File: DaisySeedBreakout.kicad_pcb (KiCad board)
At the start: 2 copper layers, 56.1 x 65 mm, 200 parts, among them J1 Conn_01x03, J10 Conn_01x02, J11 Conn_01x02, J12 Conn_01x02, J13 Conn_01x02, J14 Conn_01x02, J2 Conn_01x02, J20 Conn_01x02, J21 Conn_01x02, J22 Conn_01x02, J24 Conn_01x02, J25 Conn_01x02, J26 Conn_02x04, J27 Conn_01x03, J3 Conn_01x03, J30 Conn_01x02, J31 Conn_02x04, J32 Conn_01x02, J33 Conn_01x02, J34 Conn_01x02, J35 Conn_01x02, J4 5027740891, J47 Conn_01x03, J48 Conn_01x03, J49 Conn_01x03, J50 Conn_01x03, J51 Conn_01x03, J52 Conn_01x03, J53 Conn_01x03, J54 Conn_01x03, J55 Conn_01x03, J56 Conn_01x03, J57 Conn_01x03, J58 Conn_01x03, J59 Conn_01x03, J6 Conn_01x02, J60 Conn_01x03, J61 Conn_01x03, J62 Conn_01x03, J63 Conn_01x03, J64 Conn_01x03, J65 Conn_01x03, J67 Conn_01x02, J68 Conn_01x02, J69 Conn_01x02, J70 Conn_01x02, J8 Conn_01x02, J9 Conn_01x02, U1 H11L1M, U10 TPD2EUSB30ADRTR, U11 TPS560200DBVR, U2 PAM8320RDR, U4 ATMEGA1608-MFR, U5 MAX9814, U6 DSC6001CE2A-010.0000, U7 TLV9062IDR

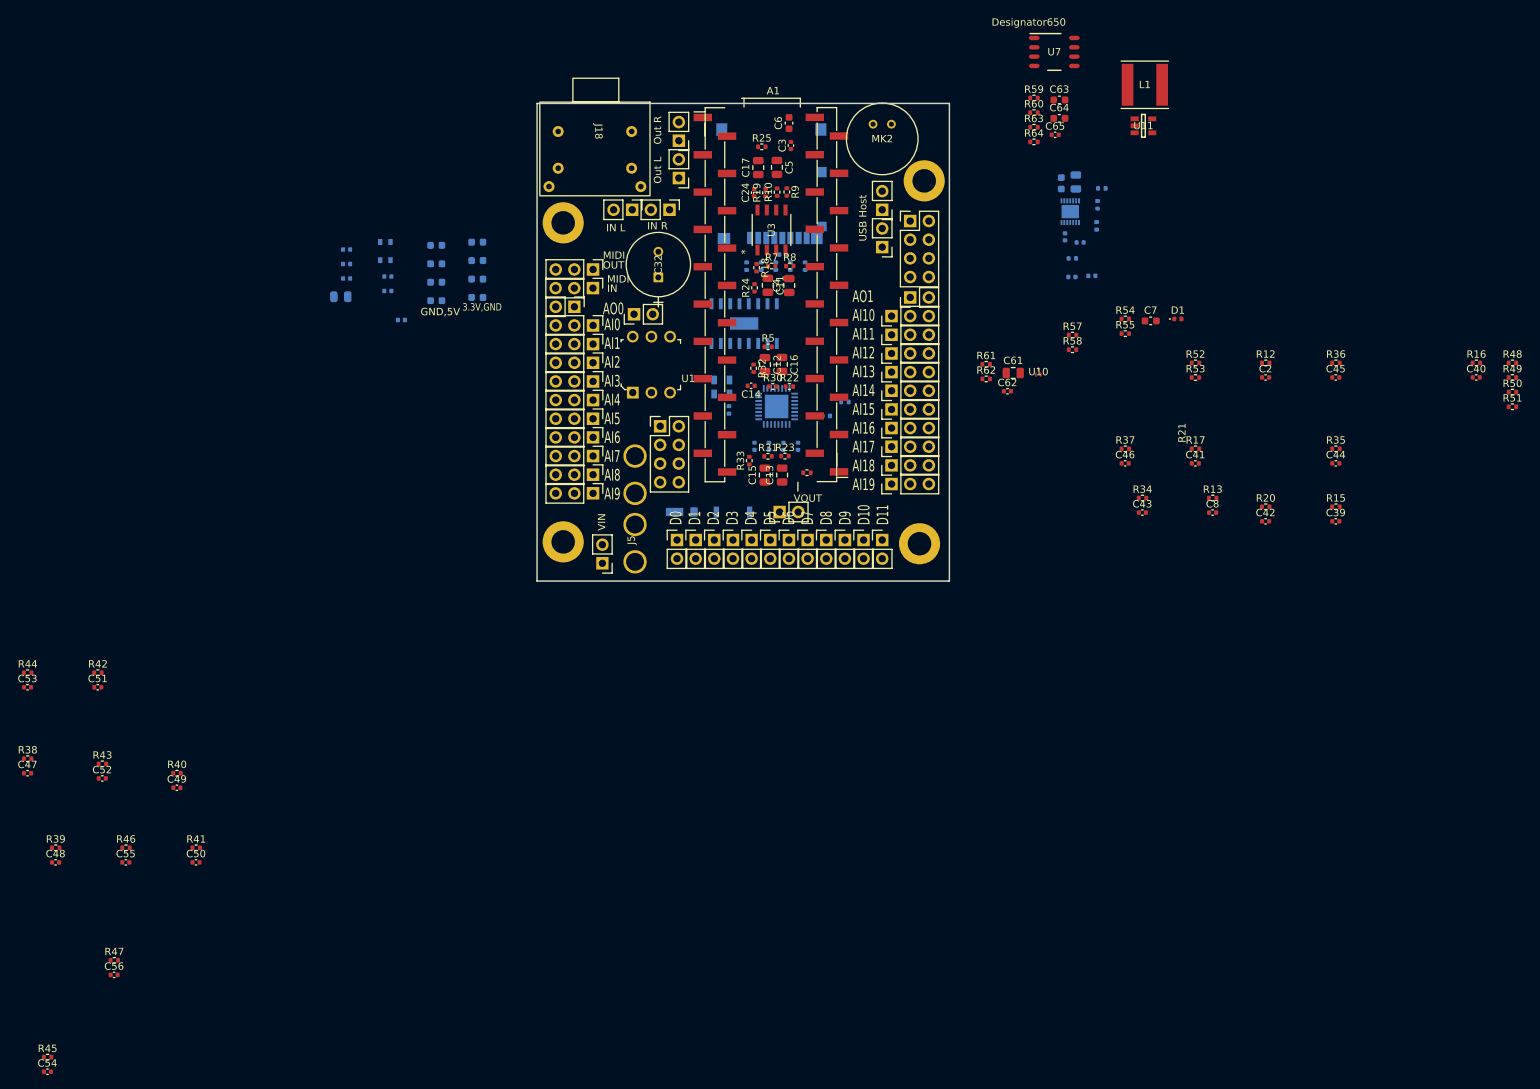
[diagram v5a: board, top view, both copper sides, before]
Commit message: Update Audio out to switch between 1V ptp or 10V ptp based on jumper
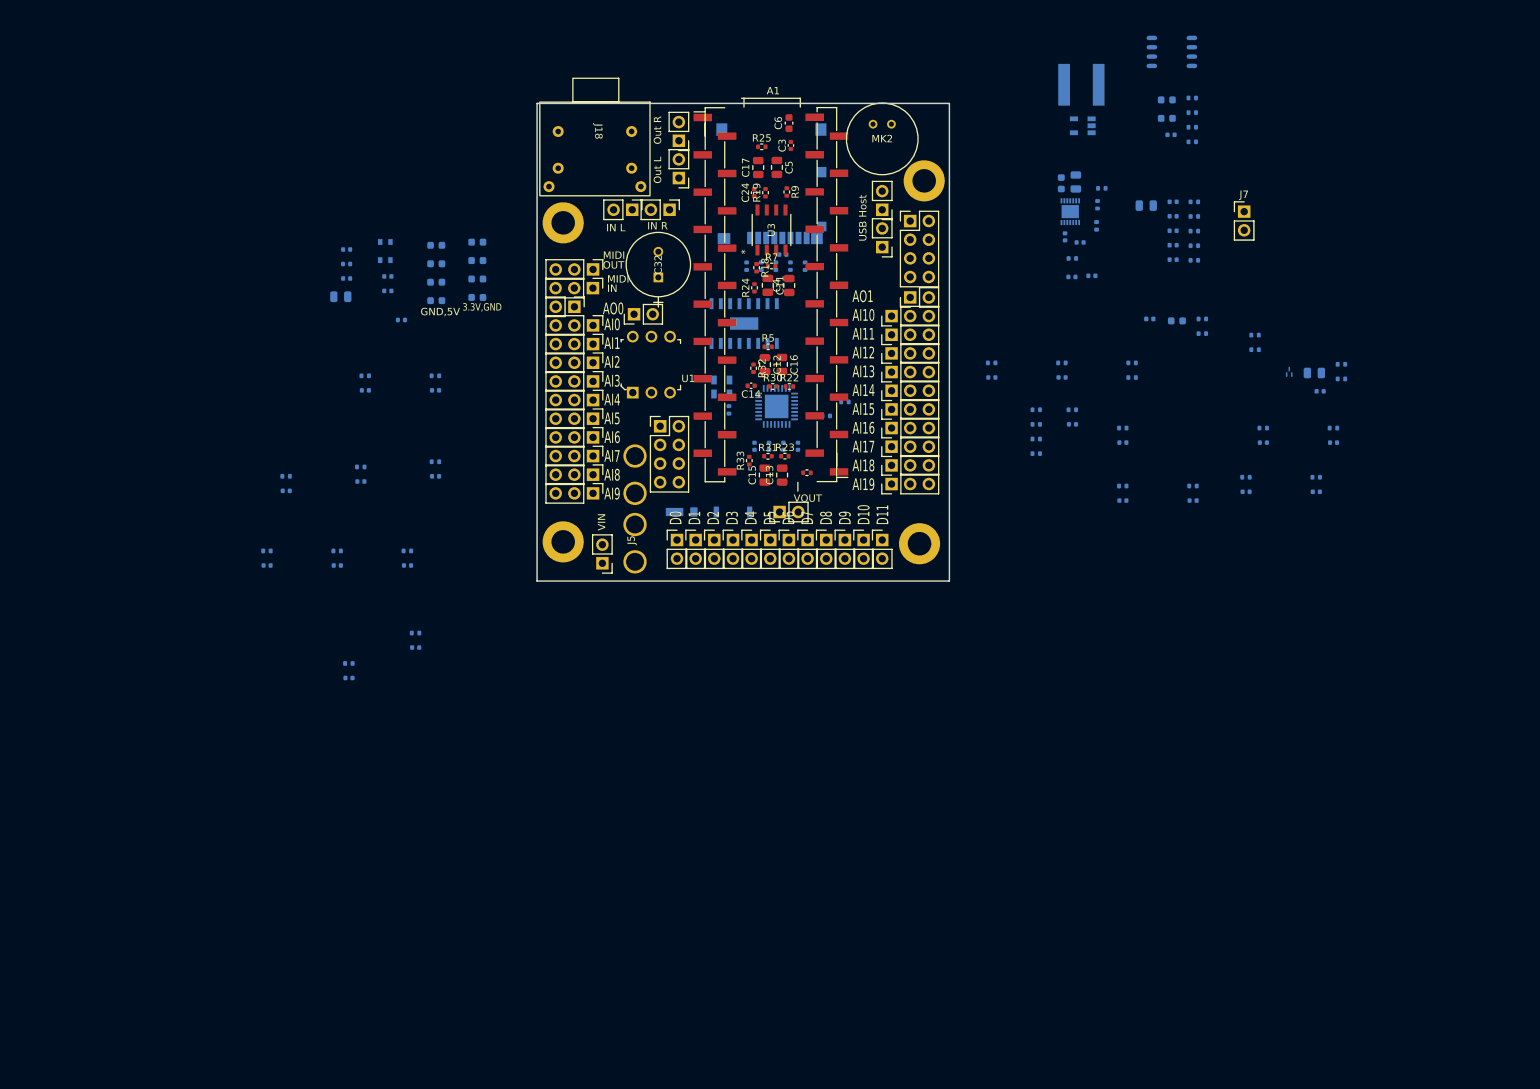
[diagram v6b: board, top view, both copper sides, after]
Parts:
- added C66: 0.1uF, Capacitor_SMD:C_0402_1005Metric, B.Cu at (194.5, 45.4)
- added C67: 10U, Capacitor_SMD:C_0805_2012Metric, B.Cu at (190.9, 45.9)
- added C68: 0.1uF, Capacitor_SMD:C_0402_1005Metric, B.Cu at (194.5, 47.4)
- added C69: 0.1uF, Capacitor_SMD:C_0402_1005Metric, B.Cu at (194.5, 49.3)
- added C70: DNP, Capacitor_SMD:C_0402_1005Metric, B.Cu at (194.5, 51.3)
- added C71: DNP, Capacitor_SMD:C_0402_1005Metric, B.Cu at (194.5, 53.3)
- added J7: Conn_01x02, Connector_PinHeader_2.54mm:PinHeader_1x02_P2.54mm_Vertical, F.Cu at (204.2, 46.7)
- added R65: 120k, Resistor_SMD:R_0402_1005Metric, B.Cu at (197.4, 49.4)
- added R66: 90k, Resistor_SMD:R_0402_1005Metric, B.Cu at (197.4, 51.4)
- added R67: 10k, Resistor_SMD:R_0402_1005Metric, B.Cu at (197.4, 53.4)
- C2, C39, C40, C41, C42, C43, C44, C45, C46, C47, C48, C49, C50, C51, C52, C53, C54, C55, C56, C61, C62, C63, C64, C65, C7, C8, D1, L1, R12, R13, R15, R16, R17, R20, R34, R35, R36, R37, R38, R39, R40, R41, R42, R43, R44, R45, R46, R47, R48, R49, R50, R51, R52, R53, R54, R55, R57, R58, R59, R60, R61, R62, R63, R64, U10, U11, U7: moved to B.Cu
- R10: value 2M -> 10k; moved to B.Cu
- R8: value 2M -> 90k; moved to B.Cu
- moved C54 76.5 mm to (91.4, 106.1), turned to 180 degrees
- moved R45 76.4 mm to (91.4, 104.1), turned to 180 degrees
- moved C47 68.7 mm to (94.1, 82.8), turned to 180 degrees
- moved C53 68.7 mm to (94.1, 71.1), turned to 180 degrees
- moved R44 68.7 mm to (94.1, 69.1), turned to 180 degrees
- moved R38 68.7 mm to (94.1, 80.8), turned to 180 degrees
- moved R48 65.1 mm to (175.9, 73.7), turned to 180 degrees
- moved R49 65.1 mm to (175.9, 75.7), turned to 180 degrees
- moved R50 65.1 mm to (175.9, 77.7), turned to 180 degrees
- moved R51 65.1 mm to (175.9, 79.7), turned to 180 degrees
- moved C48 62.7 mm to (90.3, 94.9), turned to 180 degrees
- moved R39 62.7 mm to (90.3, 92.9), turned to 180 degrees
- moved R10 56.9 mm to (197.4, 47.4), turned to 180 degrees
- moved R8 55.8 mm to (197.4, 45.4), turned to 180 degrees
- moved R16 55.4 mm to (180.8, 73.7), turned to 180 degrees
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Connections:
- R10 pad 1: Net-(U3B-+IN_B) -> /Audio Out/ENABLE_10V_EURO_N
- R10 pad 2: GND -> Net-(U3B--B)
- R18 pad 1: Net-(U3A--A) -> Net-(R18-Pad1)
- R19 pad 1: Net-(U3B--B) -> Net-(R19-Pad1)
- R7 pad 1: +12V -> /Audio Out/6V_REF
- R8 pad 1: Net-(U3A-+IN_A) -> Net-(U3A--A)
- R8 pad 2: GND -> Net-(R18-Pad1)
- R9 pad 1: +12V -> /Audio Out/6V_REF
- U3 pad 1: Net-(U3A--A) -> Net-(R18-Pad1)
- U3 pad 7: Net-(U3B--B) -> Net-(R19-Pad1)

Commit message: getting closer
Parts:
- removed C23, C67: 10U, Capacitor_SMD:C_0805_2012Metric
- removed C61: 47uF, Capacitor_SMD:C_0805_2012Metric
- removed C62, C65, C66, C68, C69: 0.1uF, Capacitor_SMD:C_0402_1005Metric
- removed C63, C64: 10uF, Capacitor_SMD:C_0603_1608Metric
- removed J26: Conn_02x04, Connector_PinHeader_2.54mm:PinHeader_2x04_P2.54mm_Vertical
- removed J32, J33, J34: Conn_01x02, Ultralibrarian:PinHeader_1x02_P2.54mm_Vertical_Female
- removed J7: Conn_01x02, Connector_PinHeader_2.54mm:PinHeader_1x02_P2.54mm_Vertical
- removed L1: 10uH 1.9A ASPI-0628-100M-T1, 10uHInductor:ASPI-0628_ASPI-0628-4R7M-T1_ABR
- removed R63, R64: TBD, Resistor_SMD:R_0402_1005Metric
- removed U11: TPS560200DBVR, USB_Switcher:DBV0005A_N
- added J15: Conn_01x03, Ultralibrarian:PinHeader_1x03_P2.54mm_Vertical_Female, F.Cu at (155.4, 45.5)
- added J16: Conn_02x04, Connector_PinHeader_2.54mm:PinHeader_2x04_P2.54mm_Vertical, F.Cu at (125.0, 76.7)
- added R56: 0, Resistor_SMD:R_0402_1005Metric, F.Cu at (138.6, 68.9)
- C11, C17, C24, C4, C5, R18, R19, R24, R25, R7, R9, U3: moved to B.Cu
- J10, J11, J12, J13, J14, J20, J21, J22, J24, J25, J30, J35, J6, J67, J68, J69, J70, J8, J9: footprint Ultralibrarian:PinHeader_1x02_P2.54mm_Vertical_Female -> Connector_PinHeader_2.54mm:PinHeader_1x02_P2.54mm_Vertical
- R10, R67: value 10k -> 2M
- R22, R23, R30, R31: value 4M -> 2M
- R52, U7: moved to F.Cu
- R59: value TBD -> 0; moved to F.Cu
- R60: value TBD -> DNP; moved to F.Cu
- R61: value 2.2k -> DNP; moved to F.Cu
- R65: value 120k -> 0
- R66, R8: value 90k -> 0
- moved R58 83.0 mm to (123.1, 58.0), turned to 90 degrees
- moved R61 76.8 mm to (140.7, 69.0), turned to 0 degrees
- moved R67 76.5 mm to (120.9, 51.8), turned to -90 degrees
- moved R57 76.0 mm to (129.7, 64.5), turned to -90 degrees
- moved R52 75.4 mm to (115.1, 52.3)
- moved R53 71.6 mm to (118.4, 57.6)
- moved C70 71.4 mm to (264.8, 38.6)
- moved C71 71.4 mm to (264.8, 40.5)
- moved R66 71.4 mm to (267.7, 38.6)
- moved R8 71.4 mm to (267.7, 32.7)
- moved U7 67.0 mm to (140.0, 64.2), turned to 90 degrees
- moved R10 66.9 mm to (130.7, 51.0), turned to -90 degrees
- moved R59 64.3 mm to (139.4, 59.5), turned to 0 degrees
- moved R65 64.1 mm to (133.7, 56.2)
- moved R60 60.6 mm to (143.4, 61.3), turned to 90 degrees
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- renumbered R56 to Z56
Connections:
- C13 pad 2: Net-(U7A-IN-) -> Net-(U7A-IN+)
- C15 pad 2: Net-(U7A-IN-) -> Net-(U7A-IN+)
- C22 pad 1: +5V -> +3.3VA
- C24 pad 1: +12V -> /Audio Out/VCC
- C28 pad 2: Net-(U2-IN) -> Net-(C28-Pad2)
- H1 pad 1: (no net) -> GND
- H2 pad 1: (no net) -> GND
- H3 pad 1: (no net) -> GND
- H4 pad 1: (no net) -> GND
- R10 pad 1: /Audio Out/ENABLE_10V_EURO_N -> Net-(U3A-+IN_A)
- R10 pad 2: Net-(U3B--B) -> GND
- R23 pad 1: Net-(U7A-IN-) -> Net-(U7A-IN+)
- R29 pad 2: Net-(C23-Pad1) -> Net-(U5-MICOUT)
- R31 pad 2: Net-(U7A-IN-) -> Net-(U7A-IN+)
- R32 pad 2: Net-(U7B-IN-) -> Net-(U7B-OUT)
- R33 pad 2: Net-(U7A-IN+) -> Net-(U7A-OUT)
- R59 pad 1: +12V -> Net-(U7B-OUT)
- R59 pad 2: Net-(U11-EN) -> Net-(U7B-IN-)
- R60 pad 1: Net-(U11-EN) -> Net-(U7B-IN-)
- R61 pad 1: +5V -> Net-(U7A-IN-)
- R65 pad 1: +12V -> Net-(C28-Pad2)
- R65 pad 2: /Audio Out/6V_REF -> Net-(U2-IN)
- R67 pad 1: /Audio Out/ENABLE_10V_EURO_N -> Net-(U3B-+IN_B)
- R67 pad 2: Net-(U3A--A) -> GND
- R7 pad 1: /Audio Out/6V_REF -> /Audio Out/VCC
- R9 pad 1: /Audio Out/6V_REF -> /Audio Out/VCC
- U3 pad 8: +12V -> /Audio Out/VCC
- U5 pad 10: +5V -> +3.3VA
- U5 pad 2: +5V -> +3.3VA
- U5 pad 5: +5V -> +3.3VA
- U7 pad 1: Net-(U7A-IN+) -> Net-(U7A-OUT)
- U7 pad 7: Net-(U7B-IN-) -> Net-(U7B-OUT)
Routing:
- net /Audio In Sum/AUDIO_IN_L_CONN: track 0.00 -> 37.8 mm
- net /Audio In Sum/AUDIO_IN_R_CONN: track 0.00 -> 29.3 mm
- net Net-(U7A-IN+): track 0.00 -> 29.2 mm
- net /MIDI_UART_TX: track 0.00 -> 27.8 mm
- net /Audio In Sum/AUDIO_IN_R_SUMMED: track 0.00 -> 21.2 mm
- net /AO1: track 0.00 -> 13.4 mm
- net Net-(U7B-IN+): track 0.00 -> 9.30 mm
- net Net-(U7B-IN-): track 0.00 -> 7.30 mm
- net /MIDI_UART_RX: track 0.00 -> 6.29 mm
- net Net-(U7B-OUT): track 0.00 -> 5.55 mm
- net Net-(J1-Pin_2): track 0.00 -> 5.46 mm
- net Net-(U7A-OUT): track 0.00 -> 3.76 mm
- net /Audio In Sum/AUDIO_IN_L_SUMMED: track 0.00 -> 3.57 mm
- net Net-(U7A-IN-): track 0.00 -> 3.21 mm
- net /AO0: track 0.00 -> 3.07 mm
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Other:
- board text added: "GND,VOUT"
- board text added: "IN L,R"
- board text added: "Out L,R"
- board text added: "SPKR"
- board text removed: "GND,5V"
- board text removed: "IN L"
- board text removed: "IN R"
- board text removed: "Out R"

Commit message: getting closer
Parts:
- C2, C39, C40, C41, C42, C43, C44, C45, C46, C8, R12, R13, R15, R16, R17, R20, R34, R35, R36, R37, R48, R49, R50, R51: moved to F.Cu
- moved C43 77.1 mm to (137.9, 72.9)
- moved R34 73.3 mm to (141.5, 72.6), turned to 0 degrees
- moved C41 68.9 mm to (137.9, 76.2), turned to -90 degrees
- moved R17 67.6 mm to (139.2, 76.2), turned to -90 degrees
- moved C8 63.5 mm to (141.0, 84.1), turned to -90 degrees
- moved R13 62.2 mm to (142.2, 84.1), turned to -90 degrees
- moved C42 56.7 mm to (141.5, 75.9), turned to -90 degrees
- moved R20 55.1 mm to (142.7, 75.9), turned to -90 degrees
- moved C39 50.3 mm to (137.7, 81.0), turned to -90 degrees
- moved R15 48.8 mm to (138.9, 81.0), turned to -90 degrees
- moved J69 45.7 mm to (158.8, 61.0), turned to 90 degrees
- moved C2 44.5 mm to (137.4, 84.1), turned to -90 degrees
- moved R12 44.0 mm to (138.7, 84.1), turned to -90 degrees
- moved J47 40.8 mm to (156.2, 83.8), turned to 90 degrees
- moved J48 40.8 mm to (156.2, 81.3), turned to 90 degrees
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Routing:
- net Net-(J48-Pin_2): track 0.00 -> 28.5 mm
- net Net-(J27-Pin_2): track 0.00 -> 21.8 mm
- net Net-(J47-Pin_2): track 0.00 -> 17.3 mm
- net /AI3: track 0.00 -> 13.2 mm
- net /AI6: track 0.00 -> 12.9 mm
- net /AI5: track 0.00 -> 11.8 mm
- net /AI1: track 0.00 -> 11.8 mm
- net /AI0: track 0.00 -> 11.0 mm
- net /AI4: track 0.00 -> 10.9 mm
- net /AI2: track 0.00 -> 10.6 mm
- net /AO0: track 3.07 -> 10.1 mm
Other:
- board text removed: "VOUT"
